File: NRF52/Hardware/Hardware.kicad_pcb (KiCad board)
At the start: 2 copper layers, 23 parts, among them J1 USB_C_Receptacle_USB2.0, J2 1.54 E-INK, Q1 AO3401A, Q2 AO3400A, U1 nRF52840, U2 MCP1700x-180xxTT, Y1 32MHz 8pF ±10ppm, Y2 32.768kHz 6pF ±20ppm

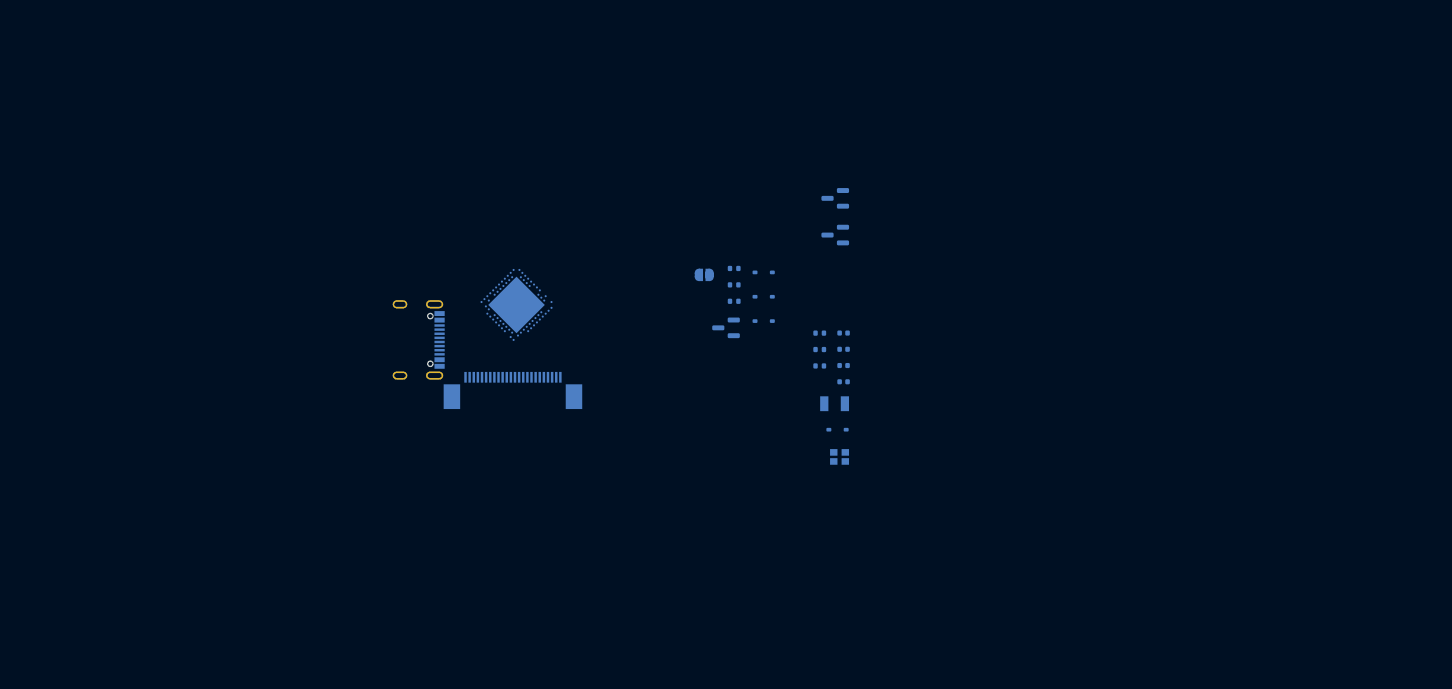
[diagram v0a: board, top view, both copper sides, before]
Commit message: Progress on NRF52 version hardware
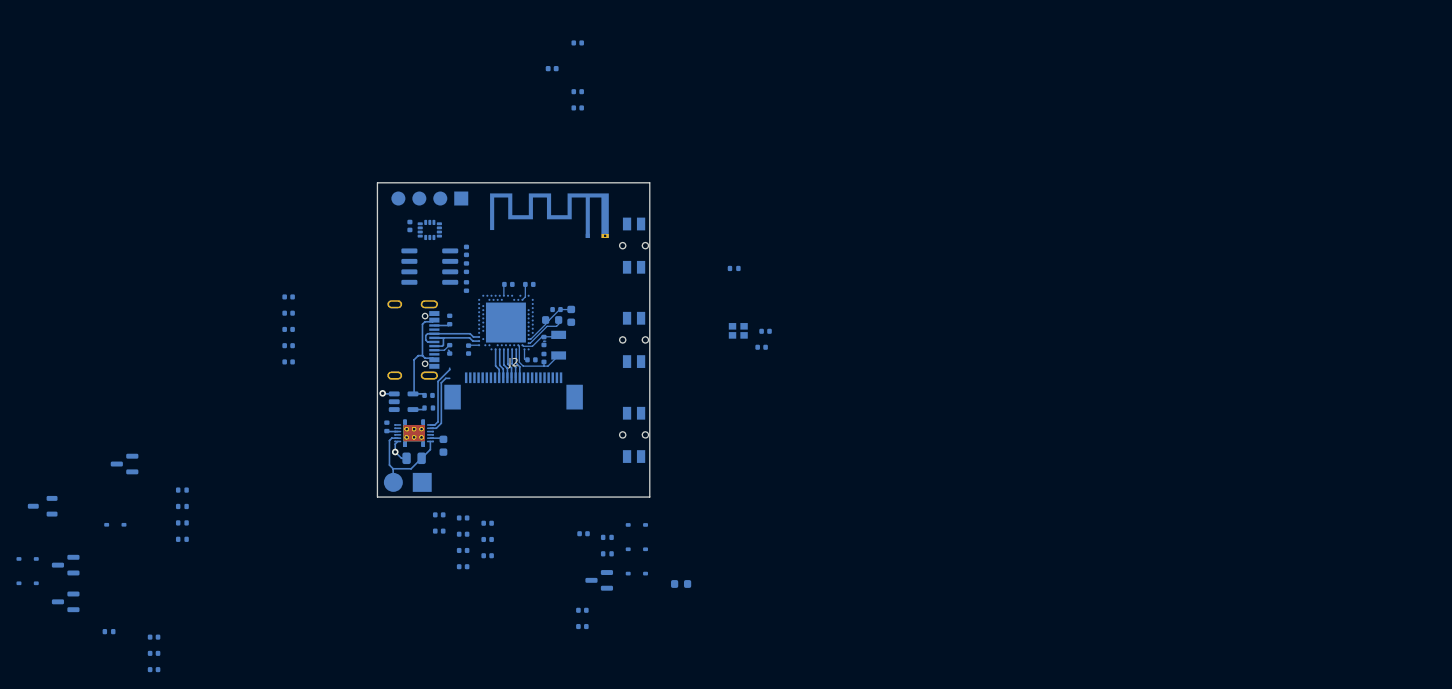
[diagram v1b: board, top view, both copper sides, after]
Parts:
- removed JP1: Jumper_2_Open, Jumper:SolderJumper-2_P1.3mm_Open_RoundedPad1.0x1.5mm
- added AE1: Antenna_PCB, RF_Antenna:Texas_SWRA117D_2.4GHz_Right, B.Cu at (110.0, 88.3)
- added C1: 1u, Capacitor_SMD:C_0402_1005Metric, B.Cu at (106.2, 97.3)
- added C10: 4u7, Capacitor_SMD:C_0402_1005Metric, B.Cu at (108.7, 72.8)
- added C11: 4u7, Capacitor_SMD:C_0402_1005Metric, B.Cu at (95.5, 102.1)
- added C12: 1u, Capacitor_SMD:C_0402_1005Metric, B.Cu at (73.7, 95.8)
- added C13: 4u7, Capacitor_SMD:C_0402_1005Metric, B.Cu at (73.7, 97.7)
- added C14: 100n, Capacitor_SMD:C_0402_1005Metric, B.Cu at (73.7, 99.7)
- added C15: 100n, Capacitor_SMD:C_0402_1005Metric, B.Cu at (73.7, 101.7)
- added C18: 100n, Capacitor_SMD:C_0402_1005Metric, B.Cu at (73.7, 103.6)
- added C19: 4u7, Capacitor_SMD:C_0402_1005Metric, B.Cu at (109.3, 133.7)
- added C20: 4u7, Capacitor_SMD:C_0402_1005Metric, B.Cu at (109.3, 135.7)
- added C21: 4u7, Capacitor_SMD:C_0402_1005Metric, B.Cu at (109.4, 124.5)
- added C22: 4u7, Capacitor_SMD:C_0402_1005Metric, B.Cu at (94.8, 122.6)
- added C23: 1u, Capacitor_SMD:C_0402_1005Metric, B.Cu at (94.8, 124.5)
- added C24: 4u7, Capacitor_SMD:C_0402_1005Metric, B.Cu at (94.8, 126.5)
- added C25: 4u7, Capacitor_SMD:C_0402_1005Metric, B.Cu at (94.8, 128.5)
- added C26: 1u, Capacitor_SMD:C_0402_1005Metric, B.Cu at (97.8, 123.2)
- added C27: 1u, Capacitor_SMD:C_0402_1005Metric, B.Cu at (97.8, 125.2)
- added C28: 4u7, Capacitor_SMD:C_0402_1005Metric, B.Cu at (97.8, 127.1)
- added C29: 4u7, Capacitor_SMD:C_0402_1005Metric, B.Cu at (91.9, 122.2)
- added C30: 1u, Capacitor_SMD:C_0402_1005Metric, B.Cu at (91.9, 124.1)
- added C31: 1u, Capacitor_SMD:C_0402_1005Metric, B.Cu at (90.7, 107.7)
- added C32: 470n, Capacitor_SMD:C_0603_1608Metric, B.Cu at (92.5, 113.8)
- added C33: 100n, Capacitor_SMD:C_0402_1005Metric, B.Cu at (57.4, 137.0)
- added C34: 1u, Capacitor_SMD:C_0402_1005Metric, B.Cu at (57.4, 139.0)
- added C35: 1u, Capacitor_SMD:C_0402_1005Metric, B.Cu at (57.4, 140.9)
- added C36: 1u, Capacitor_SMD:C_0402_1005Metric, B.Cu at (88.4, 87.2)
- added C37: 1u, Capacitor_SMD:C_0402_1005Metric, B.Cu at (95.2, 90.2)
- added C4: 47n, Capacitor_SMD:C_0603_1608Metric, B.Cu at (108.0, 98.0)
- added C5: 820p, Capacitor_SMD:C_0402_1005Metric, B.Cu at (100.3, 94.2)
- added C6: 0p5, Capacitor_SMD:C_0402_1005Metric, B.Cu at (108.7, 65.0)
- added C7: 100p, Capacitor_SMD:C_0402_1005Metric, B.Cu at (102.9, 94.2)
- added C8: 100n, Capacitor_SMD:C_0402_1005Metric, B.Cu at (103.1, 103.4)
- added C9: 0p8, Capacitor_SMD:C_0402_1005Metric, B.Cu at (108.7, 70.9)
- added D5: 1N5819WS, Diode_SMD:D_SOD-323, B.Cu at (42.0, 127.5)
- added D6: 1N5819WS, Diode_SMD:D_SOD-323, B.Cu at (42.0, 130.5)
- added J3: Conn_01x04, local:Program_Pads, B.Cu at (94.6, 83.8)
- added J4: Battery, local:Battery Pads, B.Cu at (88.1, 118.2)
- added L1: 4n7, Inductor_SMD:L_0402_1005Metric, B.Cu at (105.6, 68.1)
- added L2: 10u, Inductor_SMD:L_0603_1608Metric, B.Cu at (121.3, 130.6)
- added L3: 15u, Inductor_SMD:L_0603_1608Metric, B.Cu at (105.6, 98.6)
- added Q3: AO3400A, Package_TO_SOT_SMD:SOT-23, B.Cu at (46.7, 128.3)
- added Q4: AO3401A, Package_TO_SOT_SMD:SOT-23, B.Cu at (46.7, 132.7)
- added R10: 100K, Resistor_SMD:R_0402_1005Metric, B.Cu at (60.8, 119.2)
- added R11: 1M, Resistor_SMD:R_0402_1005Metric, B.Cu at (60.8, 121.2)
- added R12: 10K, Resistor_SMD:R_0402_1005Metric, B.Cu at (60.8, 123.2)
- added R13: 10K, Resistor_SMD:R_0402_1005Metric, B.Cu at (60.8, 125.1)
- added R14: 10K, Resistor_SMD:R_0402_1005Metric, B.Cu at (95.2, 94.5)
- added R15: 10K, Resistor_SMD:R_0402_1005Metric, B.Cu at (95.2, 92.2)
- added R7: R01 1%, Resistor_SMD:R_0805_2012Metric, B.Cu at (88.9, 115.3)
- added R8: 10K, Resistor_SMD:R_0402_1005Metric, B.Cu at (85.6, 111.5)
- added R9: 2K2, Resistor_SMD:R_0402_1005Metric, B.Cu at (90.7, 109.2)
- added SW1: SW_Push, Button_Switch_SMD:Panasonic_EVQPUL_EVQPUC, B.Cu at (115.6, 101.0)
- added SW2: SW_Push, Button_Switch_SMD:Panasonic_EVQPUL_EVQPUC, B.Cu at (115.6, 89.5)
- added SW3: SW_Push, Button_Switch_SMD:Panasonic_EVQPUL_EVQPUC, B.Cu at (115.6, 112.5)
- added U3: BQ27441DRZR-G1A, Package_SON:Texas_S-PDSO-N12, B.Cu at (88.9, 112.3)
- added U4: XC6206PxxxMR, Package_TO_SOT_SMD:SOT-23-3, B.Cu at (43.9, 121.1)
- added U5: LSM6DS3, Package_LGA:LGA-14_3x2.5mm_P0.5mm_LayoutBorder3x4y, B.Cu at (90.8, 87.6)
- added U6: DS3231MZ, Package_SO:SOIC-8_3.9x4.9mm_P1.27mm, B.Cu at (90.8, 92.1)
- J2: moved to B.Cu
- R3, R4: value 100K -> 10K
- U2: value MCP1700x-180xxTT -> TP4054; footprint Package_TO_SOT_SMD:SOT-23 -> Package_TO_SOT_SMD:SOT-23-5
- moved Q1 92.0 mm to (53.8, 116.0)
- moved R3 92.0 mm to (51.9, 136.3)
- moved D1 88.3 mm to (52.7, 123.4)
- moved U2 56.1 mm to (87.6, 108.5), turned to 0 degrees
- moved R1 44.9 mm to (93.2, 98.5), turned to 90 degrees
- moved R2 44.9 mm to (93.2, 102.1), turned to -90 degrees
- moved C16 36.4 mm to (104.6, 101.1), turned to 90 degrees
- moved C17 36.4 mm to (104.6, 103.2), turned to 90 degrees
- moved Q2 34.3 mm to (111.3, 130.1)
- moved D2 34.3 mm to (115.9, 123.4)
- moved D3 34.3 mm to (115.9, 126.3)
- moved R5 34.3 mm to (112.3, 124.9)
- moved R6 34.3 mm to (112.3, 126.9)
- moved D4 34.3 mm to (115.9, 129.3)
- moved Y2 34.2 mm to (106.4, 101.6), turned to -90 degrees
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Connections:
- J2 pad 15: +1V8 -> +3V3
- J2 pad 16: +1V8 -> +3V3
- Q1 pad 3: +BATT -> Net-(Q1-D)
- R4 pad 2: +1V8 -> +3V3
- U1 pad A10: /EINK_SDI -> unconnected-(U1-AIN5/P0.29-PadA10)
- U1 pad A22: +1V8 -> +3V3
- U1 pad A8: /EINK_SCLK -> unconnected-(U1-AIN7/P0.31-PadA8)
- U1 pad AA24: unconnected-(U1-SWDCLK-PadAA24) -> /SWDCLK
- U1 pad AC11: unconnected-(U1-P0.16-PadAC11) -> /POWER_LATCH
- U1 pad AC24: unconnected-(U1-SWDIO-PadAC24) -> /SWDIO
- U1 pad AC9: unconnected-(U1-P0.14-PadAC9) -> /DOWN_BUTTON
- U1 pad AD10: unconnected-(U1-P0.15-PadAD10) -> /POWER_BUTTON
- U1 pad AD12: unconnected-(U1-P0.17-PadAD12) -> /VBUS_PRESENT
- U1 pad AD14: +1V8 -> +3V3
- U1 pad AD16: unconnected-(U1-P0.20-PadAD16) -> /RTC_INT
- U1 pad AD18: unconnected-(U1-P0.22-PadAD18) -> /IMU_INT
- U1 pad AD20: unconnected-(U1-P0.24-PadAD20) -> /SDA
- U1 pad AD22: unconnected-(U1-TRACEDATA0/P1.00-PadAD22) -> /SCL
- U1 pad AD23: +1V8 -> +3V3
- U1 pad AD8: unconnected-(U1-P0.13-PadAD8) -> /UP_BUTTON
- U1 pad B1: +1V8 -> +3V3
- U1 pad B11: /EINK_DC -> unconnected-(U1-AIN4/P0.28-PadB11)
- U1 pad B17: unconnected-(U1-P1.12-PadB17) -> /EINK_DC
- U1 pad B9: /EINK_CS -> unconnected-(U1-AIN6/P0.30-PadB9)
- U1 pad G1: /EINK_RES -> /EINK_SDI
- U1 pad H2: /EINK_BUSY -> unconnected-(U1-P0.27-PadH2)
- U1 pad J1: unconnected-(U1-AIN2/P0.04-PadJ1) -> /EINK_SCLK
- U1 pad L1: unconnected-(U1-P0.06-PadL1) -> /EINK_CS
- U1 pad M2: unconnected-(U1-TRACECLK/P0.07-PadM2) -> /RTC_INT
- U1 pad N1: unconnected-(U1-P0.08-PadN1) -> /EINK_DC
- U1 pad R1: unconnected-(U1-TRACEDATA3/P1.09-PadR1) -> /EINK_RES
- U1 pad U1: unconnected-(U1-TRACEDATA1/P0.12-PadU1) -> /EINK_BUSY
- U1 pad W1: +1V8 -> +3V3
- U1 pad Y2: +1V8 -> +3V3
- U2 pad 1: GND -> unconnected-(U2-~{CHRG}-Pad1)
- U2 pad 2: +1V8 -> GND
- U2 pad 3: Net-(D1-K) -> +BATT
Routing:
- net VBUS: track 0.00 -> 15.3 mm
- net Net-(J4-Pin_2): track 0.00 -> 12.9 mm
- net /USB_DN: track 0.00 -> 8.73 mm
- net /USB_DP: track 0.00 -> 8.41 mm
- net /SDA: track 0.00 -> 8.17 mm
- net Net-(U1-XL2/P0.01): track 0.00 -> 8.12 mm
- net /SCL: track 0.00 -> 7.73 mm
- net Net-(U1-DEC4): track 0.00 -> 6.96 mm
- net Net-(U1-DCC): track 0.00 -> 5.10 mm
- net Net-(U1-XL1/P0.00): track 0.00 -> 5.01 mm
- net +BATT: track 0.00 -> 4.53 mm, vias 0 -> 2
- net /EINK_SDI: track 0.00 -> 3.62 mm
- net /EINK_SCLK: track 0.00 -> 3.62 mm
- net /EINK_RES: track 0.00 -> 3.62 mm
- net /EINK_DC: track 0.00 -> 3.62 mm
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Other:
- board outline added: 33 x 38.1 mm

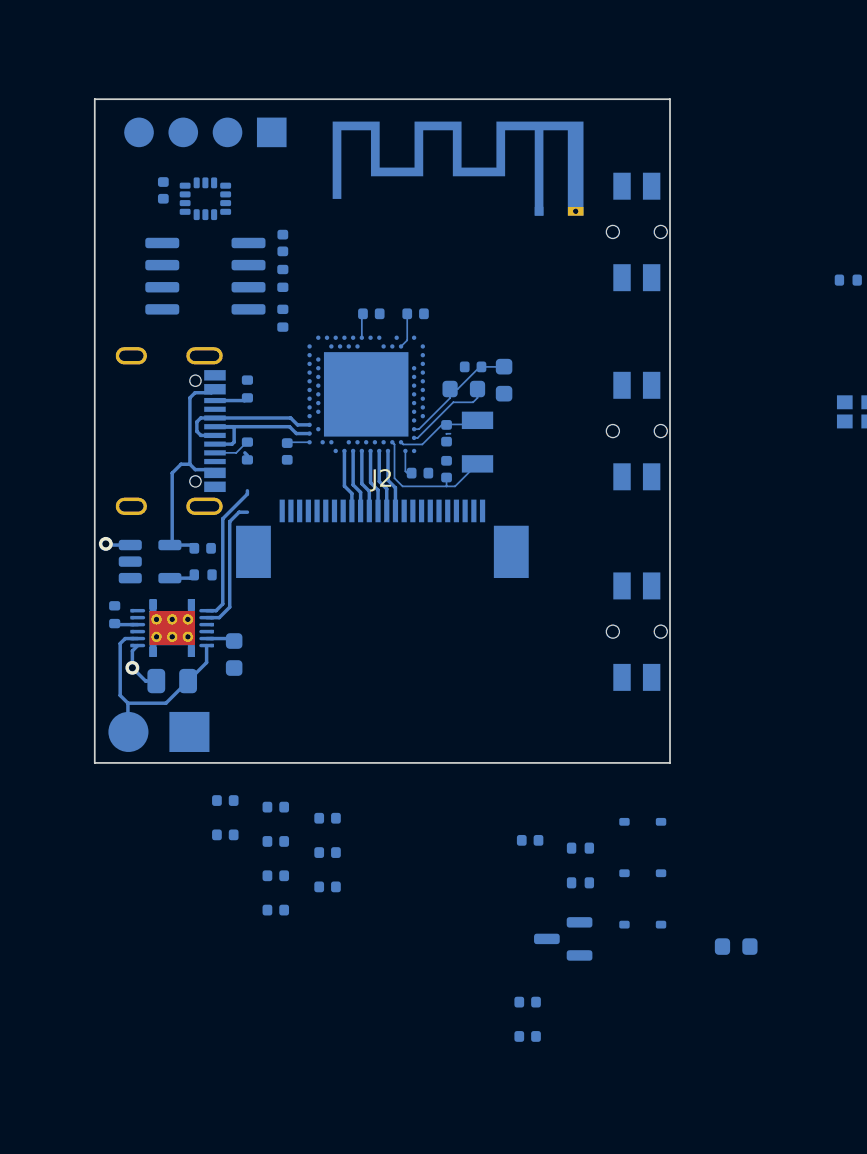
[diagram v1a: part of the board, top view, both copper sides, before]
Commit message: Correct e-ink driver components
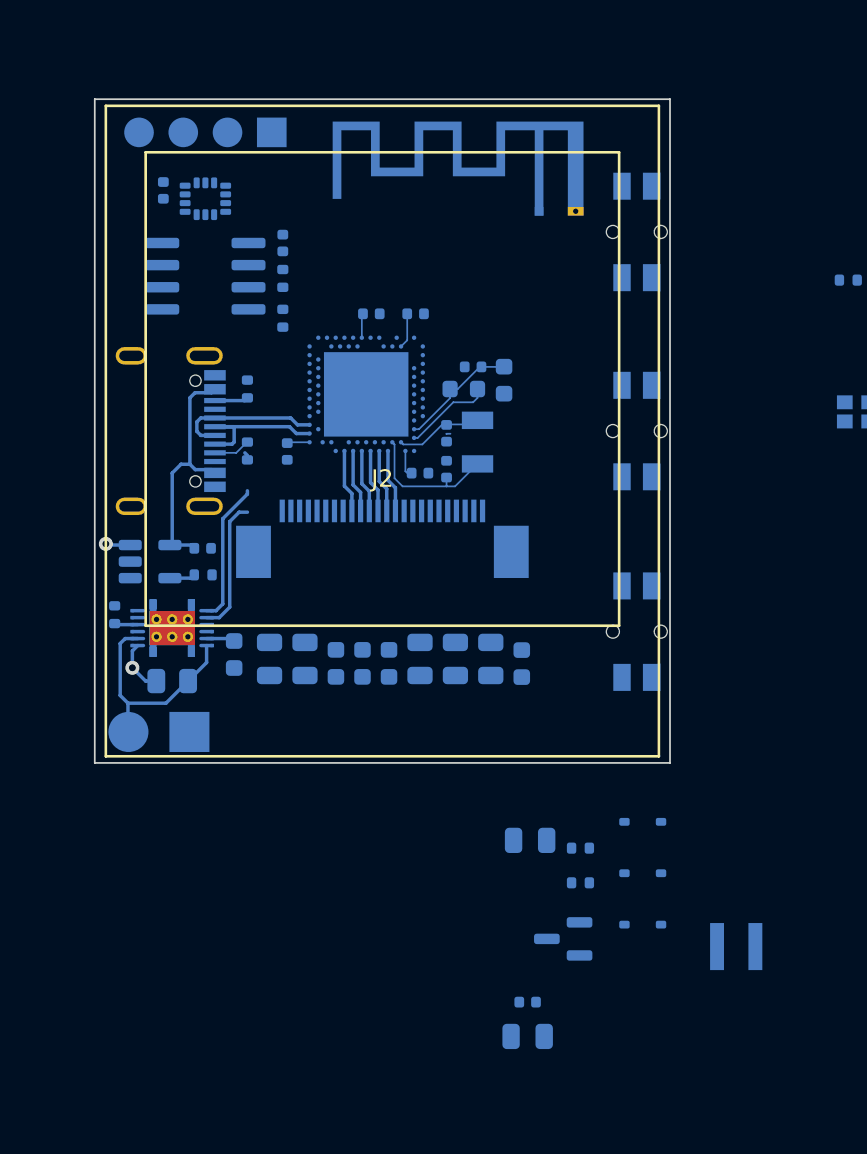
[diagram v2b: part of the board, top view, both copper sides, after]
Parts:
- C20, C21, C22, C24, C25, C28, C29: footprint Capacitor_SMD:C_0402_1005Metric -> Capacitor_SMD:C_0805_2012Metric
- C23, C26, C27, C30: footprint Capacitor_SMD:C_0402_1005Metric -> Capacitor_SMD:C_0603_1608Metric
- L2: footprint Inductor_SMD:L_0603_1608Metric -> Inductor_SMD:L_Taiyo-Yuden_MD-3030
- moved C30 19.7 mm to (109.0, 114.3), turned to -90 degrees
- moved C24 17.5 mm to (107.2, 114.0), turned to -90 degrees
- moved C29 15.5 mm to (105.2, 114.0), turned to -90 degrees
- moved C25 14.5 mm to (96.5, 114.0), turned to -90 degrees
- moved C28 14.1 mm to (103.1, 114.0), turned to -90 degrees
- moved C23 12.1 mm to (101.3, 114.3), turned to -90 degrees
- moved C27 11.0 mm to (99.8, 114.3), turned to -90 degrees
- moved C26 8.90 mm to (98.3, 114.3), turned to -90 degrees
- moved C22 8.51 mm to (94.5, 114.0), turned to -90 degrees
